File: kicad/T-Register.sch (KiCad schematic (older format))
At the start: 19 parts, among them U17 74LS245, U18 74LS173, U19 74LS173

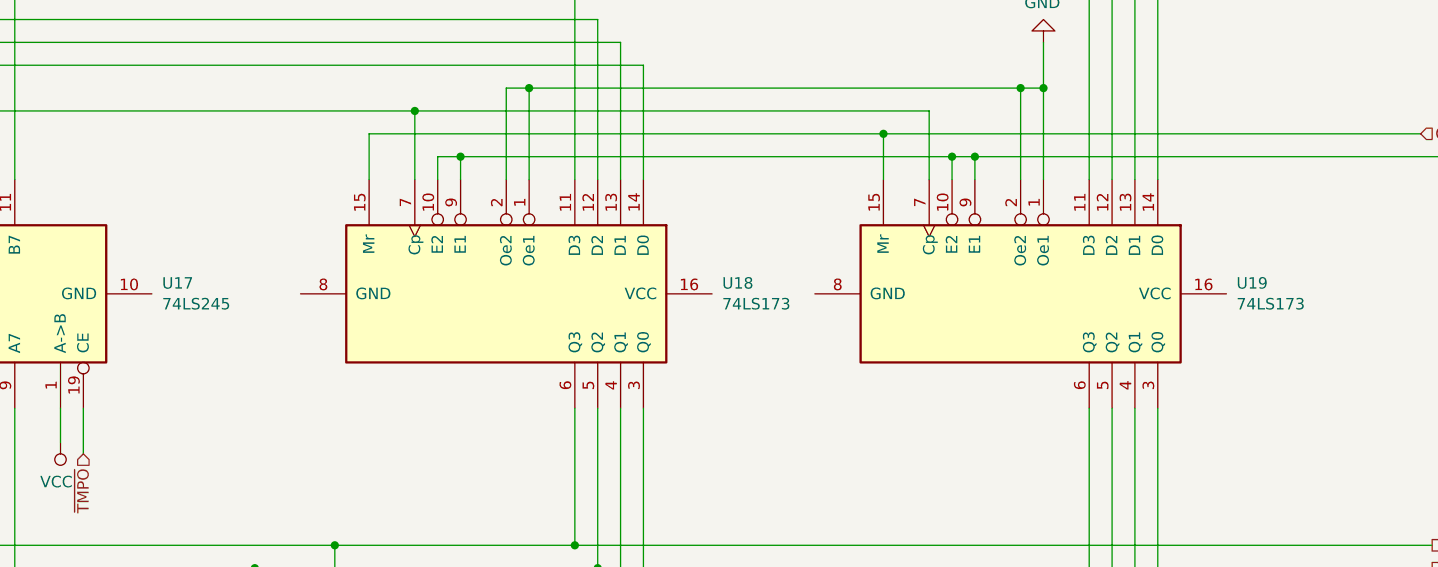
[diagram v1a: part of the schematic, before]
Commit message: Reorganize part references
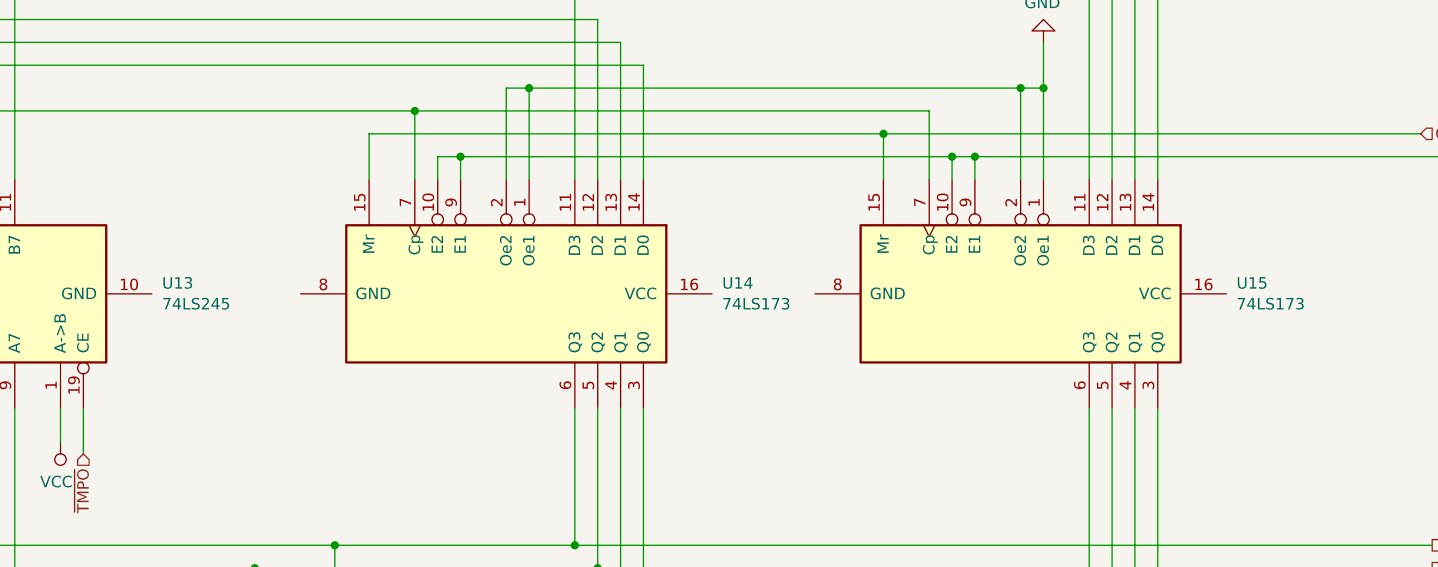
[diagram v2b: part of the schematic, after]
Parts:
- renumbered U17 to U13, U18 to U14, U19 to U15
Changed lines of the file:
@@
 $Descr USLetter 11000 8500
 encoding utf-8
-Sheet 18 26
+Sheet 5 26
 Title ""
 Date "2019-10-03"
@@
 AR Path="/5DA98D6D/5DA9A543/602273E1" Ref="U?"  Part="1"
 AR Path="/5DA9C21D/602273E1" Ref="U?"  Part="1"
-AR Path="/5E9E6254/602273E1" Ref="U17"  Part="1"
-F 0 "U17" V 2996 2706 50  0000 R CNN
+AR Path="/5E9E6254/602273E1" Ref="U13"  Part="1"
+F 0 "U13" V 2996 2706 50  0000 R CNN
 F 1 "74LS245" V 2905 2706 50  0000 R CNN
 F 2 "" H 2950 3550 50  0001 C CNN
@@
 AR Path="/5DA98D6D/5DA9A543/6022740E" Ref="U?"  Part="1"
 AR Path="/5DA9C21D/6022740E" Ref="U?"  Part="1"
-AR Path="/5E9E6254/6022740E" Ref="U19"  Part="1"
-F 0 "U19" V 7504 4494 50  0000 L CNN
+AR Path="/5E9E6254/6022740E" Ref="U15"  Part="1"
+F 0 "U15" V 7504 4494 50  0000 L CNN
 F 1 "74LS173" V 7595 4494 50  0000 L CNN
 F 2 "" H 7550 3550 50  0001 C CNN
@@
 AR Path="/5DA98D6D/5DA9A543/602274F9" Ref="U?"  Part="1"
 AR Path="/5DA9C21D/602274F9" Ref="U?"  Part="1"
-AR Path="/5E9E6254/602274F9" Ref="U18"  Part="1"
-F 0 "U18" V 5254 4494 50  0000 L CNN
+AR Path="/5E9E6254/602274F9" Ref="U14"  Part="1"
+F 0 "U14" V 5254 4494 50  0000 L CNN
 F 1 "74LS173" V 5345 4494 50  0000 L CNN
 F 2 "" H 5300 3550 50  0001 C CNN
